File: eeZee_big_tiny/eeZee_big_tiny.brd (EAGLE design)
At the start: 37.6 x 16.3 mm, 11 parts, among them IC1 ATtiny2313/4313, J2 avrisp, Q1 16MHz

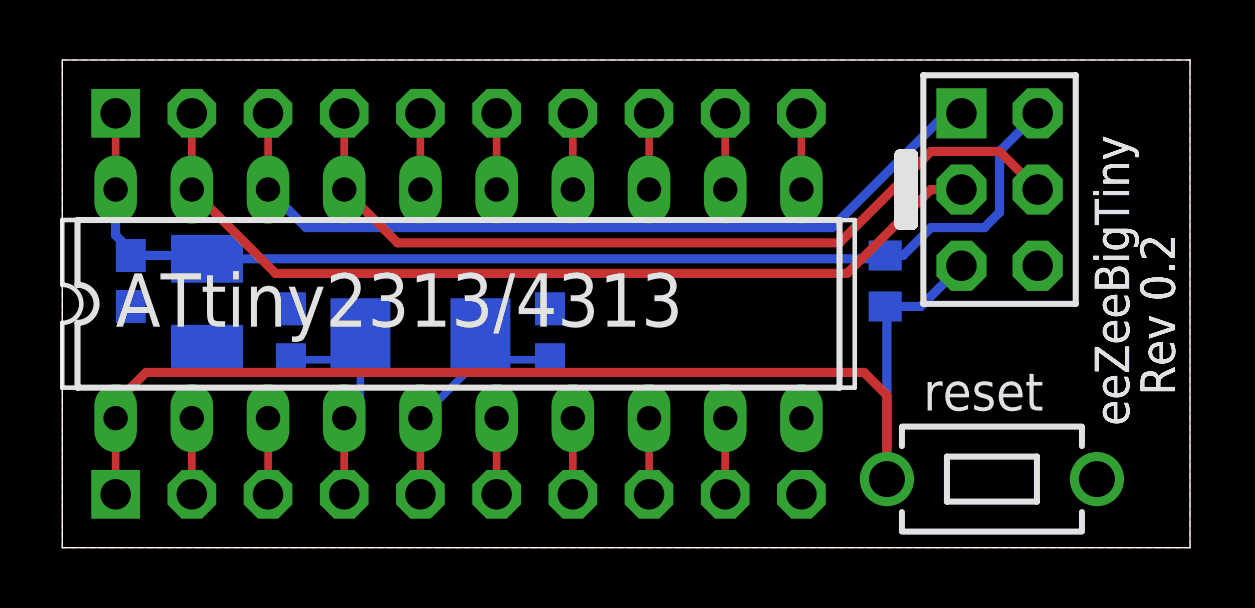
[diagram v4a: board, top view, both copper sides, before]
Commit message: Rev 0.2, mitered corners, changed silk on tantalum to indicate polarity, few minor rearrangements.
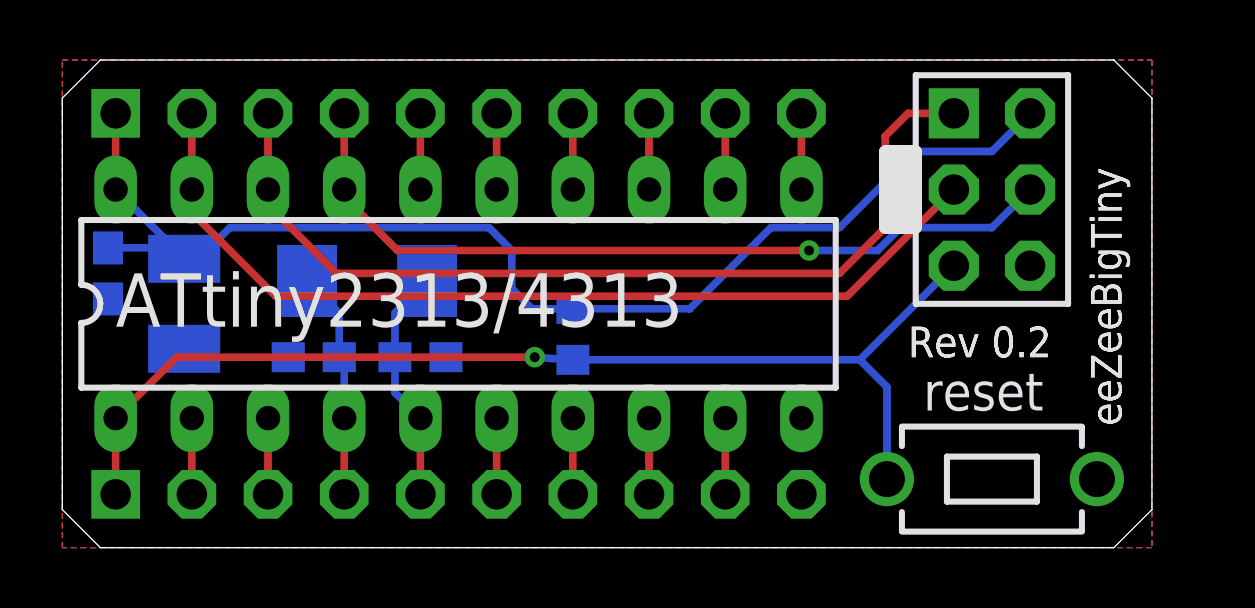
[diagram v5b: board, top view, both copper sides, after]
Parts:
- C2: device rcl:SMC_B -> mes_rcl:SMC_B
- moved R1 10.6 mm to (17.0, 7.11)
- moved C5 4.38 mm to (11.9, 6.35), turned to 180 degrees
- moved Q1 2.51 mm to (10.2, 8.89)
- moved C4 1.08 mm to (8.38, 6.35), turned to 0 degrees
- moved C1 0.80 mm to (1.52, 9.14)
- moved C2 0.76 mm to (4.06, 8.13)
- moved J2 0.25 mm to (31.0, 11.9)
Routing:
- net !RESET: track 41.2 -> 37.0 mm, vias 0 -> 1
- net N$2: track 27.8 -> 30.8 mm
- net VCC: track 38.7 -> 41.7 mm
- net N$3: track 28.2 -> 27.2 mm, vias 0 -> 1
- net XTAL1: track 8.83 -> 7.91 mm
- net N$4: track 30.5 -> 31.3 mm
- net XTAL2: track 8.23 -> 7.62 mm
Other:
- board size 37.6 x 16.3 mm -> 36.3 x 16.3 mm
- board text removed: "16MHz"
- board text removed: "C1"
- board text removed: "C2"
- board text removed: "C4"
- board text removed: "C5"
- board text removed: "R1"
